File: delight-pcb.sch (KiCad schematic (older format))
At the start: 171 parts, among them J1 AVR-ISP-6, SW0 KEYSW, SW1 KEYSW, SW10 KEYSW, SW11 KEYSW, SW12 KEYSW, SW13 KEYSW, SW14 KEYSW, SW15 KEYSW, SW16 KEYSW, SW17 KEYSW, SW18 KEYSW, SW19 KEYSW, SW2 KEYSW, SW20 KEYSW, SW21 KEYSW, SW22 KEYSW, SW23 KEYSW, SW24 KEYSW, SW25 KEYSW, SW26 KEYSW, SW27 KEYSW, SW28 KEYSW, SW28-2 KEYSW, SW29 KEYSW, SW3 KEYSW, SW30 KEYSW, SW31 KEYSW, SW32 KEYSW, SW33 KEYSW, SW34 KEYSW, SW35 KEYSW, SW36 KEYSW, SW37 KEYSW, SW38 KEYSW, SW39 KEYSW, SW4 KEYSW, SW40 KEYSW, SW41 KEYSW, SW42 KEYSW, SW42-2 KEYSW, SW43 KEYSW, SW44 KEYSW, SW44-2 KEYSW, SW45 KEYSW, SW46 KEYSW, SW47 KEYSW, SW48 KEYSW, SW49 KEYSW, SW5 KEYSW, SW50 KEYSW, SW51 KEYSW, SW52 KEYSW, SW53 KEYSW, SW54 KEYSW, SW55 KEYSW, SW56 KEYSW, SW57 KEYSW, SW58 KEYSW, SW59 KEYSW, SW59-2 KEYSW, SW6 KEYSW, SW60 KEYSW, SW60-2 KEYSW, SW61 KEYSW, SW62-2 KEYSW, SW63 KEYSW, SW63-2 KEYSW, SW64 KEYSW, SW64-2 KEYSW, SW65 KEYSW, SW65-2 KEYSW, SW66 KEYSW, SW67 KEYSW, SW68 KEYSW, SW69 KEYSW, SW7 KEYSW, SW8 KEYSW, SW9 KEYSW, U1 ATmega32A-PU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

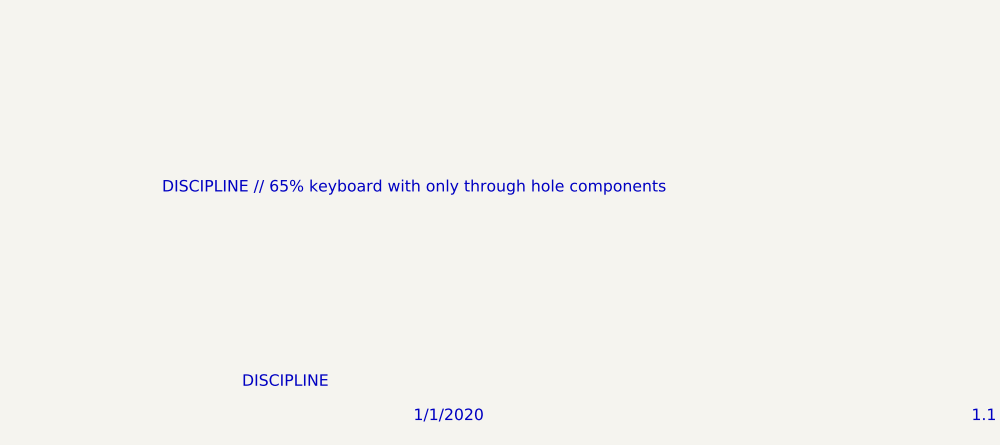
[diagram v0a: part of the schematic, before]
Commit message: Attempted Project Rename
Attempting to rename the project.
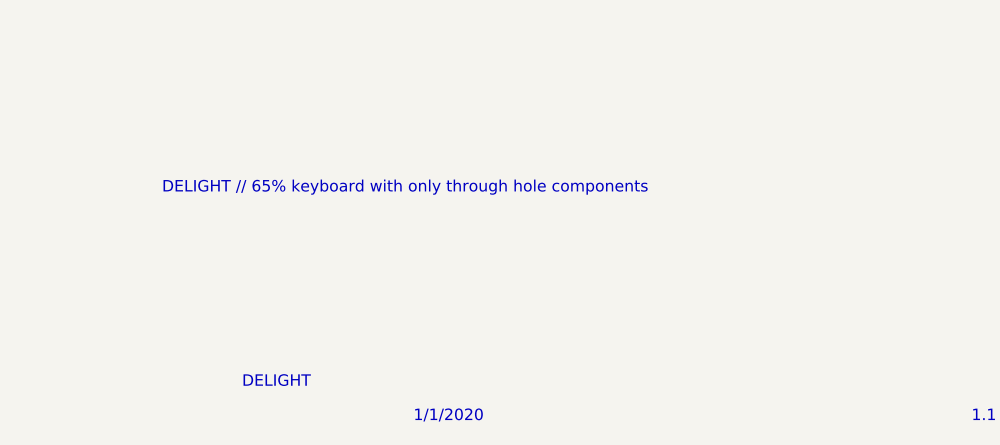
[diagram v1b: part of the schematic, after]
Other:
- note added: "DELIGHT"
- note added: "DELIGHT // 65% keyboard with only through hole components"
- note removed: "DISCIPLINE"
- note removed: "DISCIPLINE // 65% keyboard with only through hole components"
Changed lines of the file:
@@
 	3600 5250 3600 5300
 Text Notes 11900 10050 0    50   ~ 0
-DISCIPLINE // 65% keyboard with only through hole components
+DELIGHT // 65% keyboard with only through hole components
 Text Notes 13000 11050 0    50   ~ 0
 1/1/2020
 Text Notes 12250 10900 0    50   ~ 0
-DISCIPLINE
+DELIGHT
 $Comp
 L discipline-pcb-rescue:KEYSW-keyboard_parts SW66

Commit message: Renaming Continued
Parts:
- BOOT1, RESET1: symbol discipline-pcb-rescue:SW_PUSH-keyboard_parts -> delight-pcb-rescue:SW_PUSH-keyboard_parts
- C1, C2, C4, C5: symbol discipline-pcb-rescue:C_Small-Device -> delight-pcb-rescue:C_Small-Device
- C3: symbol discipline-pcb-rescue:CP1_Small-Device -> delight-pcb-rescue:CP1_Small-Device
- D0, D1, D10, D11, D12, D13, D14, D15, D16, D17, D18, D19, D2, D20, D21, D22, D23, D24, D25, D26, D27, D28, D29, D3, D30, D31, D32, D33, D34, D35, D36, D37, D38, D39, D4, D40, D41, D42, D43, D44, D45, D46, D47, D48, D49, D5, D50, D51, D52, D53, D54, D55, D56, D57, D58, D59, D6, D60, D61, D62, D63, D64, D65, D66, D67, D68, D69, D7, D8, D9: symbol discipline-pcb-rescue:D-Device -> delight-pcb-rescue:D-Device
- D70, D71: symbol discipline-pcb-rescue:D_Zener_Small-Device -> delight-pcb-rescue:D_Zener_Small-Device
- F1: symbol discipline-pcb-rescue:Polyfuse_Small-Device -> delight-pcb-rescue:Polyfuse_Small-Device
- J1: symbol discipline-pcb-rescue:AVR-ISP-6-Connector -> delight-pcb-rescue:AVR-ISP-6-Connector
- LED1: symbol discipline-pcb-rescue:LED-Device -> delight-pcb-rescue:LED-Device
- R1, R2, R3, R4, R5, R6, R7: symbol discipline-pcb-rescue:R_Small-Device -> delight-pcb-rescue:R_Small-Device
- S62, SW0, SW1, SW10, SW11, SW12, SW13, SW14, SW15, SW16, SW17, SW18, SW19, SW2, SW20, SW21, SW22, SW23, SW24, SW25, SW26, SW27, SW28, SW28-2, SW29, SW3, SW30, SW31, SW32, SW33, SW34, SW35, SW36, SW37, SW38, SW39, SW4, SW40, SW41, SW42, SW42-2, SW43, SW44, SW44-2, SW45, SW46, SW47, SW48, SW49, SW5, SW50, SW51, SW52, SW53, SW54, SW55, SW56, SW57, SW58, SW59, SW59-2, SW6, SW60, SW60-2, SW61, SW62-2, SW63, SW63-2, SW64, SW64-2, SW65, SW65-2, SW66, SW67, SW68, SW69, SW7, SW8, SW9: symbol discipline-pcb-rescue:KEYSW-keyboard_parts -> delight-pcb-rescue:KEYSW-keyboard_parts
- U1: symbol discipline-pcb-rescue:ATmega32A-PU-MCU_Microchip_ATmega -> delight-pcb-rescue:ATmega32A-PU-MCU_Microchip_ATmega
- USB1: symbol discipline-pcb-rescue:USB_C_Receptacle_USB2.0-Connector -> delight-pcb-rescue:USB_C_Receptacle_USB2.0-Connector
- Y1: symbol discipline-pcb-rescue:Crystal_Small-Device -> delight-pcb-rescue:Crystal_Small-Device
